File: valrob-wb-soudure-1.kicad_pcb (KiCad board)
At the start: 2 copper layers, 85 x 50 mm, 35 parts, among them J1 Conn_01x03, J2 Conn_01x06, J3 Conn_01x02, J4 Conn_01x02, J5 Conn_01x02, J6 Conn_01x02, Q1 2N7000, SW1 SW_Push, SW2 SW_Push, SW3 SW_Push, SW4 SW_Push

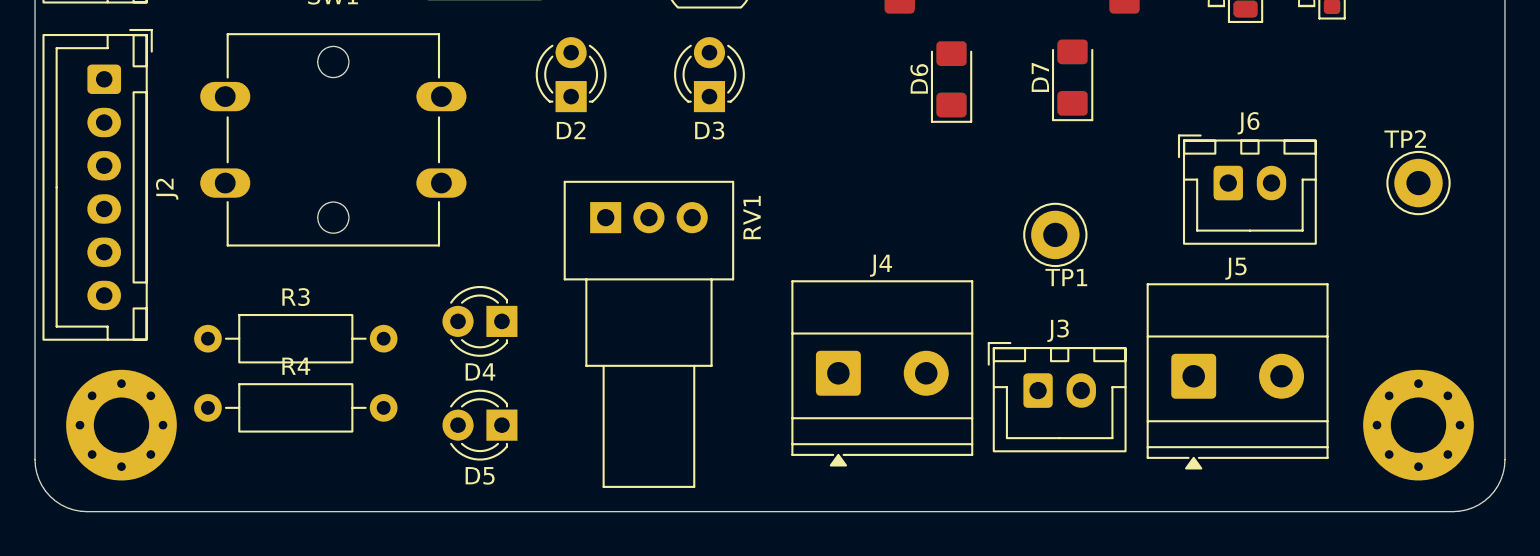
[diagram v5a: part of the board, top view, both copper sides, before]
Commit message: pcb: improve board outline
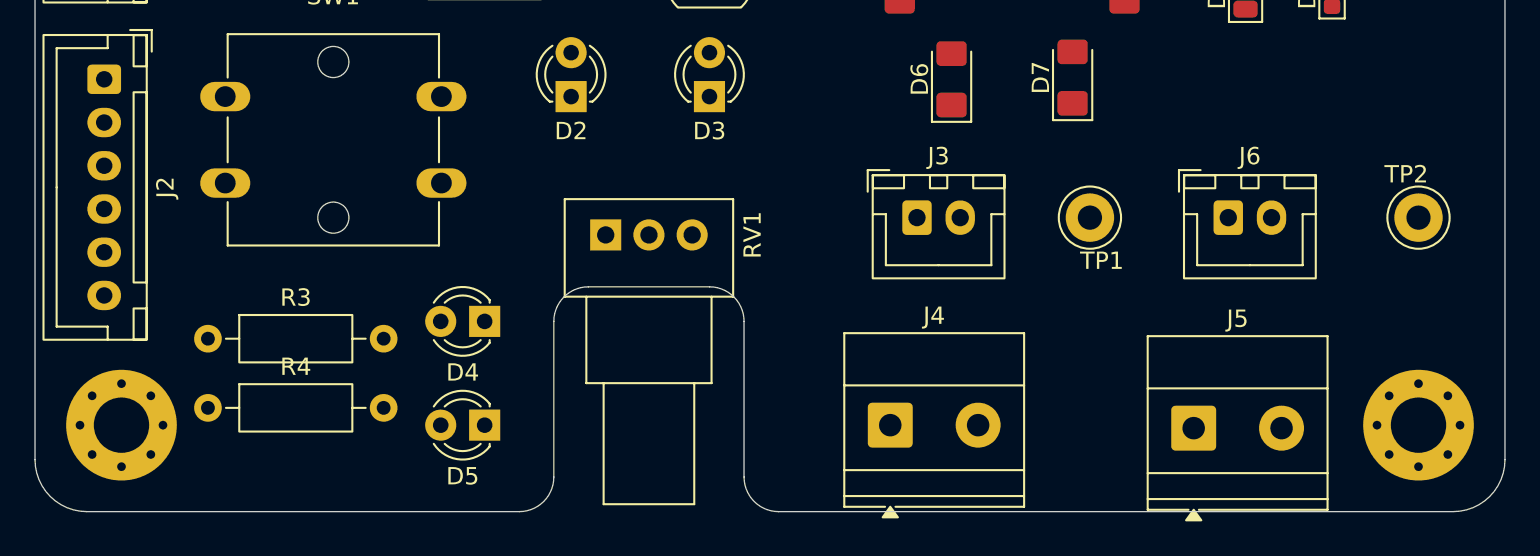
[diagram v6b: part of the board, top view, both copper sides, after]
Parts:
- moved J3 12.2 mm to (99.0, 126.0)
- moved J4 4.24 mm to (97.5, 138.0)
- moved J5 3.00 mm to (115.0, 138.2)
- moved TP1 2.24 mm to (109.0, 126.0)
- moved J6 2.00 mm to (117.0, 126.0)
- moved TP2 2.00 mm to (128.0, 126.0)
- moved D4 1.00 mm to (74.0, 132.0)
- moved D5 1.00 mm to (74.0, 138.0)
- moved RV1 1.00 mm to (81.0, 127.0)
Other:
- outline, holes or cut-outs redrawn
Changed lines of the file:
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@@
 	(footprint "TerminalBlock_Phoenix:TerminalBlock_Phoenix_MKDS-1,5-2-5.08_1x02_P5.08mm_Horizontal"
 		(layer "F.Cu")
-		(at 115 135.1725)
+		(at 115 138.1725)
 		(descr "Terminal Block Phoenix MKDS-1,5-2-5.08, 2 pins, pitch 5.08mm, size 10.2x9.8mm, drill diameter 1.3mm, pad diameter 2.6mm, http://www.farnell.com/datasheets/100425.pdf")
 		(tags "THT Terminal Block Phoenix MKDS-1,5-2-5.08 pitch 5.08mm size 10.2x9.8mm drill 1.3mm pad 2.6mm")
@@
 	(footprint "TerminalBlock_Phoenix:TerminalBlock_Phoenix_MKDS-1,5-2-5.08_1x02_P5.08mm_Horizontal"
 		(layer "F.Cu")
-		(at 94.455 135)
+		(at 97.455 138)
 		(descr "Terminal Block Phoenix MKDS-1,5-2-5.08, 2 pins, pitch 5.08mm, size 10.2x9.8mm, drill diameter 1.3mm, pad diameter 2.6mm, http://www.farnell.com/datasheets/100425.pdf")
 		(tags "THT Terminal Block Phoenix MKDS-1,5-2-5.08 pitch 5.08mm size 10.2x9.8mm drill 1.3mm pad 2.6mm")
@@
 	(footprint "Connector_JST:JST_XH_B2B-XH-A_1x02_P2.50mm_Vertical"
 		(layer "F.Cu")
-		(at 117 124)
+		(at 117 126)
 		(descr "JST XH series connector, B2B-XH-A (http://www.jst-mfg.com/product/pdf/eng/eXH.pdf)")
 		(tags "connector JST XH vertical")
@@
 	(footprint "LED_THT:LED_D3.0mm"
 		(layer "F.Cu")
-		(at 75 132 180)
+		(at 74 132 180)
 		(descr "LED, diameter 3.0mm, 2 pins, generated by kicad-footprint-generator")
 		(tags "LED")
@@
 		)
 		(point
-			(at 73.73 132)
+			(at 72.73 132)
 			(size 2)
 			(layer "F.Fab")
@@
 	(footprint "TestPoint:TestPoint_Loop_D3.50mm_Drill1.4mm_Beaded"
 		(layer "F.Cu")
-		(at 128 124 180)
+		(at 128 126 180)
 		(descr "wire loop with bead as test point, loop diameter 3.5mm, hole diameter 1.4mm")
 		(tags "test point wire loop bead")
@@
 	(footprint "TestPoint:TestPoint_Loop_D3.50mm_Drill1.4mm_Beaded"
 		(layer "F.Cu")
-		(at 107 127)
+		(at 109 126)
 		(descr "wire loop with bead as test point, loop diameter 3.5mm, hole diameter 1.4mm")
 		(tags "test point wire loop bead")
@@
 	(footprint "Connector_JST:JST_XH_B2B-XH-A_1x02_P2.50mm_Vertical"
 		(layer "F.Cu")
-		(at 106 136)
+		(at 99 126)
 		(descr "JST XH series connector, B2B-XH-A (http://www.jst-mfg.com/product/pdf/eng/eXH.pdf)")
 		(tags "connector JST XH vertical")
@@
 	(footprint "LED_THT:LED_D3.0mm"
 		(layer "F.Cu")
-		(at 75 138 180)
+		(at 74 138 180)
 		(descr "LED, diameter 3.0mm, 2 pins, generated by kicad-footprint-generator")
 		(tags "LED")
@@
 		)
 		(point
-			(at 73.73 138)
+			(at 72.73 138)
 			(size 2)
 			(layer "F.Fab")
@@
 	(footprint "Potentiometer_THT:Potentiometer_Alps_RK09Y11_Single_Horizontal"
 		(layer "F.Cu")
-		(at 81 126 90)
+		(at 81 127 90)
 		(descr "Potentiometer, horizontal, Long Life, Alps RK09Y11 Single, https://tech.alpsalpine.com/prod/e/pdf/potentiometer/rotarypotentiometers/rk09y11/rk09y11.pdf")
 		(tags "Potentiometer horizontal Alps RK09Y11 Single")
@@
 		(layer "Edge.Cuts")
 	)
+	(gr_line
+		(start 76 143)
+		(end 51 143)
+		(stroke
+			(width 0.05)
+			(type default)
+		)
+		(layer "Edge.Cuts")
+	)
 	(gr_arc
-		(start 130 93)
-		(mid 132.12132 93.87868)
-		(end 133 96)
+		(start 78 132)
+		(mid 78.585786 130.585786)
+		(end 80 130)
+		(stroke
+			(width 0.05)
+			(type default)
+		)
+		(layer "Edge.Cuts")
+	)
+	(gr_arc
+		(start 78 141)
+		(mid 77.414214 142.414214)
+		(end 76 143)
 		(stroke
 			(width 0.05)
@@
 	)
 	(gr_line
-		(start 130 143)
-		(end 51 143)
+		(start 78 141)
+		(end 78 132)
+		(stroke
+			(width 0.05)
+			(type default)
+		)
+		(layer "Edge.Cuts")
+	)
+	(gr_line
+		(start 87 130)
+		(end 80 130)
+		(stroke
+			(width 0.05)
+			(type default)
+		)
+		(layer "Edge.Cuts")
+	)
+	(gr_arc
+		(start 87 130)
+		(mid 88.414214 130.585786)
+		(end 89 132)
+		(stroke
+			(width 0.05)
+			(type default)
+		)
+		(layer "Edge.Cuts")
+	)
+	(gr_line
+		(start 89 132)
+		(end 89 141)
+		(stroke
+			(width 0.05)
+			(type default)
+		)
+		(layer "Edge.Cuts")
+	)
+	(gr_arc
+		(start 91 143)
+		(mid 89.585786 142.414214)
+		(end 89 141)
+		(stroke
+			(width 0.05)
+			(type default)
+		)
+		(layer "Edge.Cuts")
+	)
+	(gr_line
+		(start 91 143)
+		(end 130 143)
+		(stroke
+			(width 0.05)
+			(type default)
+		)
+		(layer "Edge.Cuts")
+	)
+	(gr_arc
+		(start 130 93)
+		(mid 132.12132 93.87868)
+		(end 133 96)
 		(stroke
 			(width 0.05)

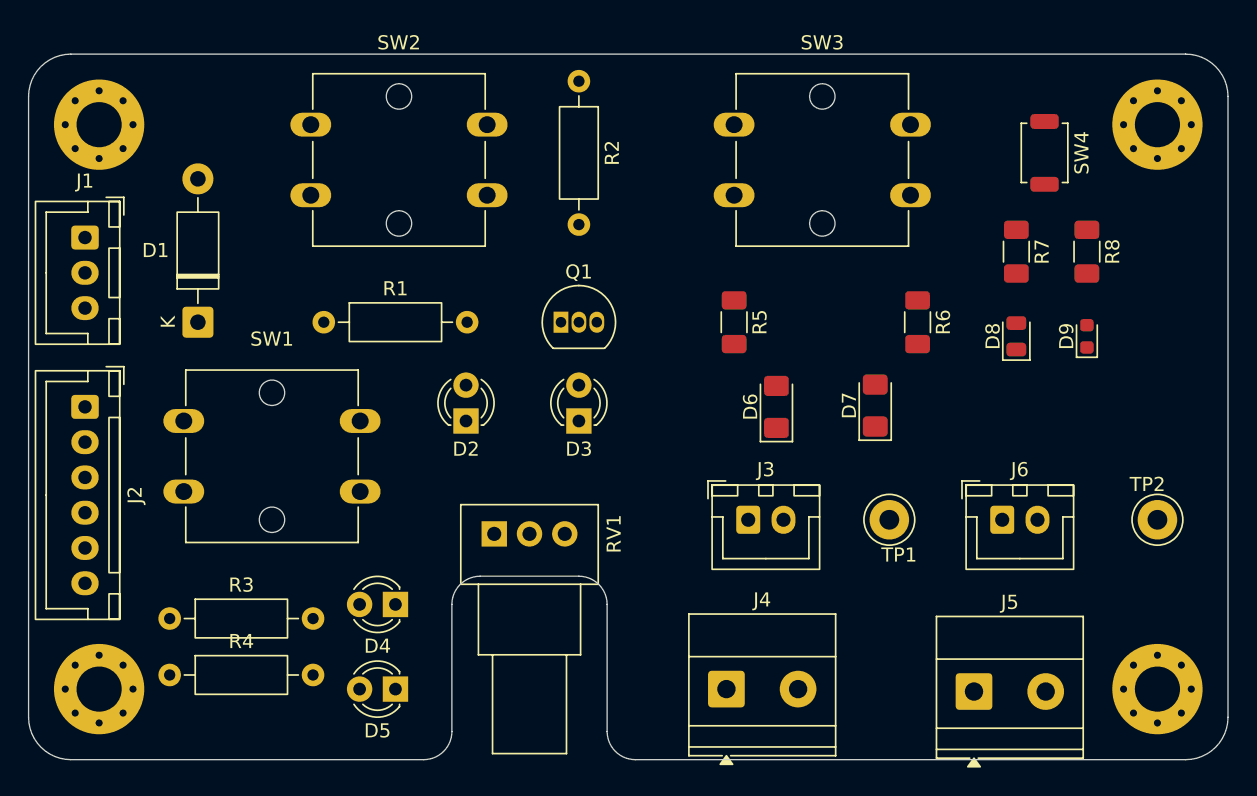
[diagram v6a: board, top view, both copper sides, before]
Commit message: pcb: add gnd planes
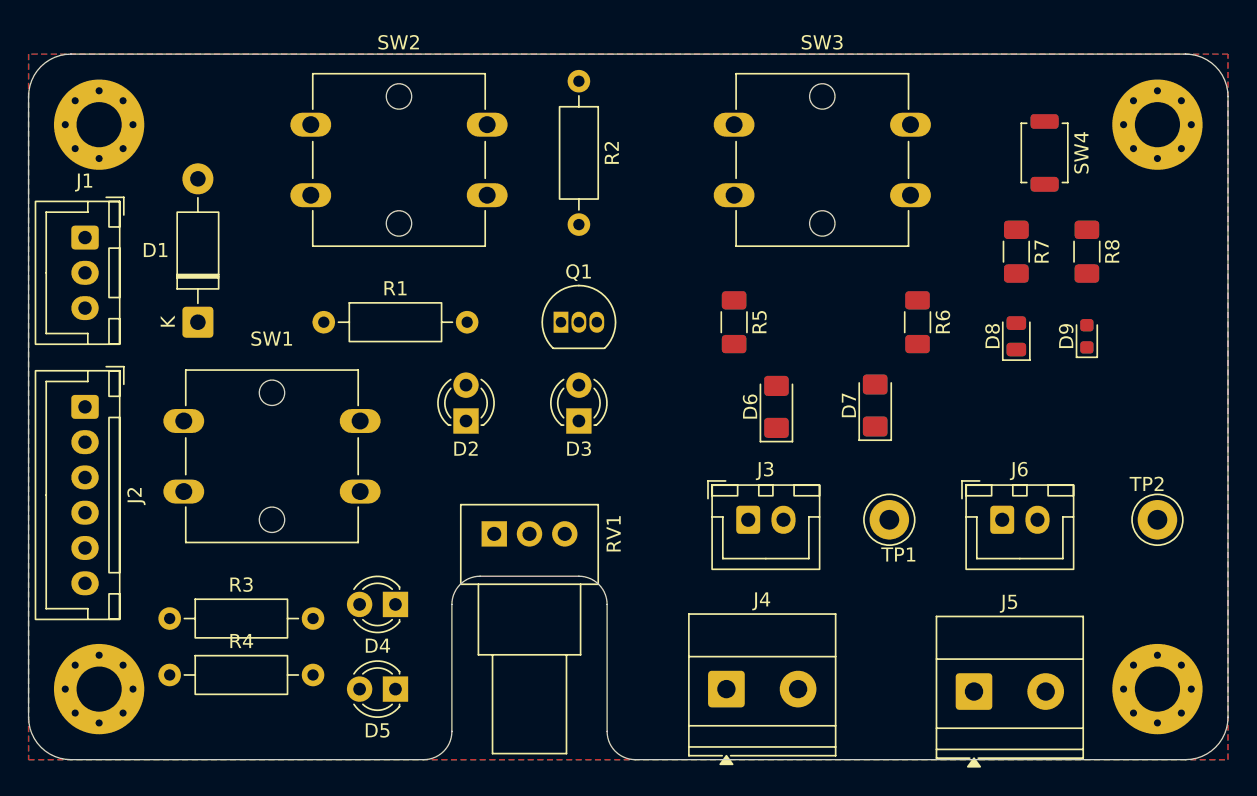
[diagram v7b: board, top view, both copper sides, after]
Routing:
- added copper zone on B.Cu, net GND
- added copper zone on F.Cu, net GND
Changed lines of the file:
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@@
 		(layer "Edge.Cuts")
+	)
+	(zone
+		(net "GND")
+		(layers "F.Cu" "B.Cu")
+		(hatch edge 0.5)
+		(connect_pads
+			(clearance 0.2)
+		)
+		(min_thickness 0.15)
+		(fill yes
+			(thermal_gap 0.35)
+			(thermal_bridge_width 0.35)
+			(island_removal_mode 0)
+		)
+		(polygon
+			(pts
+				(xy 48 93) (xy 48 143) (xy 133 143) (xy 133 93)
+			)
+		)
 	)
 	(embedded_fonts no)
